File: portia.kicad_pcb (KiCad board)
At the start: 2 copper layers, 65.1 x 56.1 mm, 46 parts, among them J1 USB_B_Micro, J11 Conn_01x02, J12 Conn_01x02, J13 Conn_01x02, J14 Conn_01x02, J3 Conn_01x02, J7 Conn_01x02, SW1 Reset, U1 CP2102N-A01-GQFN24, U4 ESP32-WROOM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

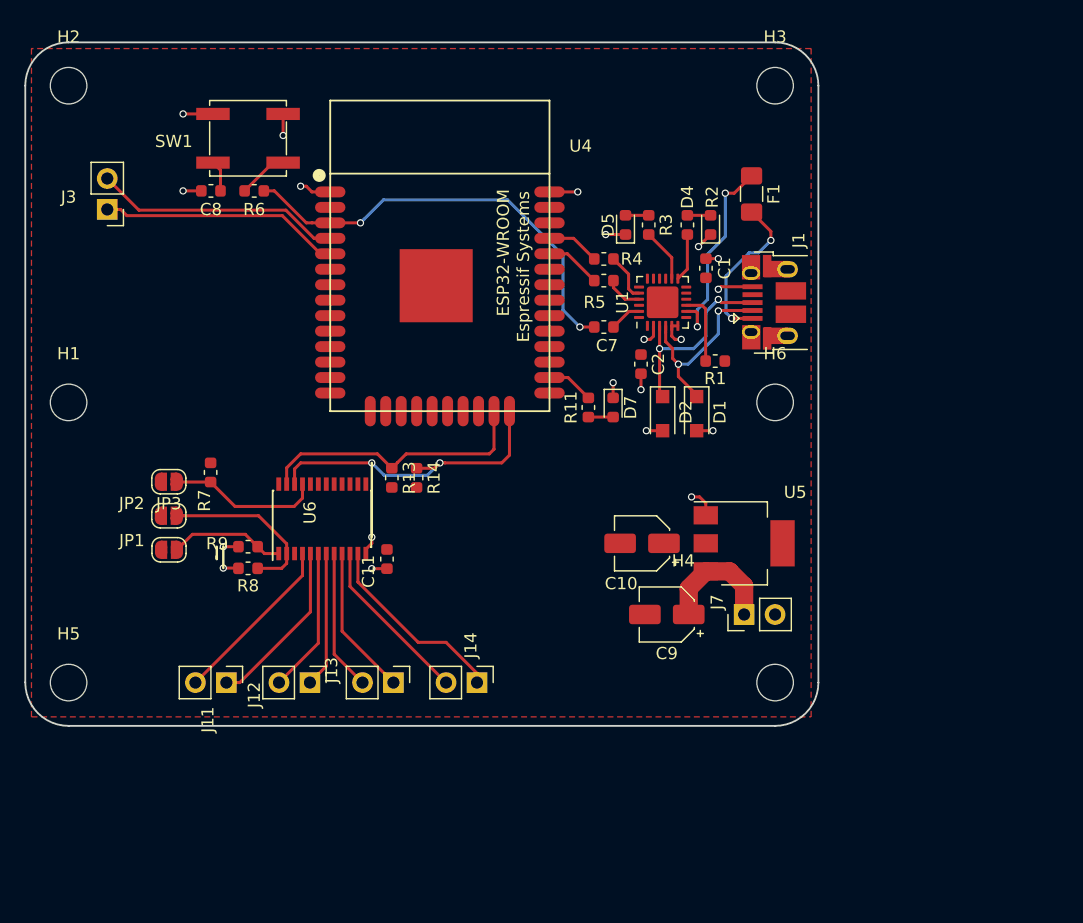
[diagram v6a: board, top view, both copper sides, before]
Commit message: adding new layout components
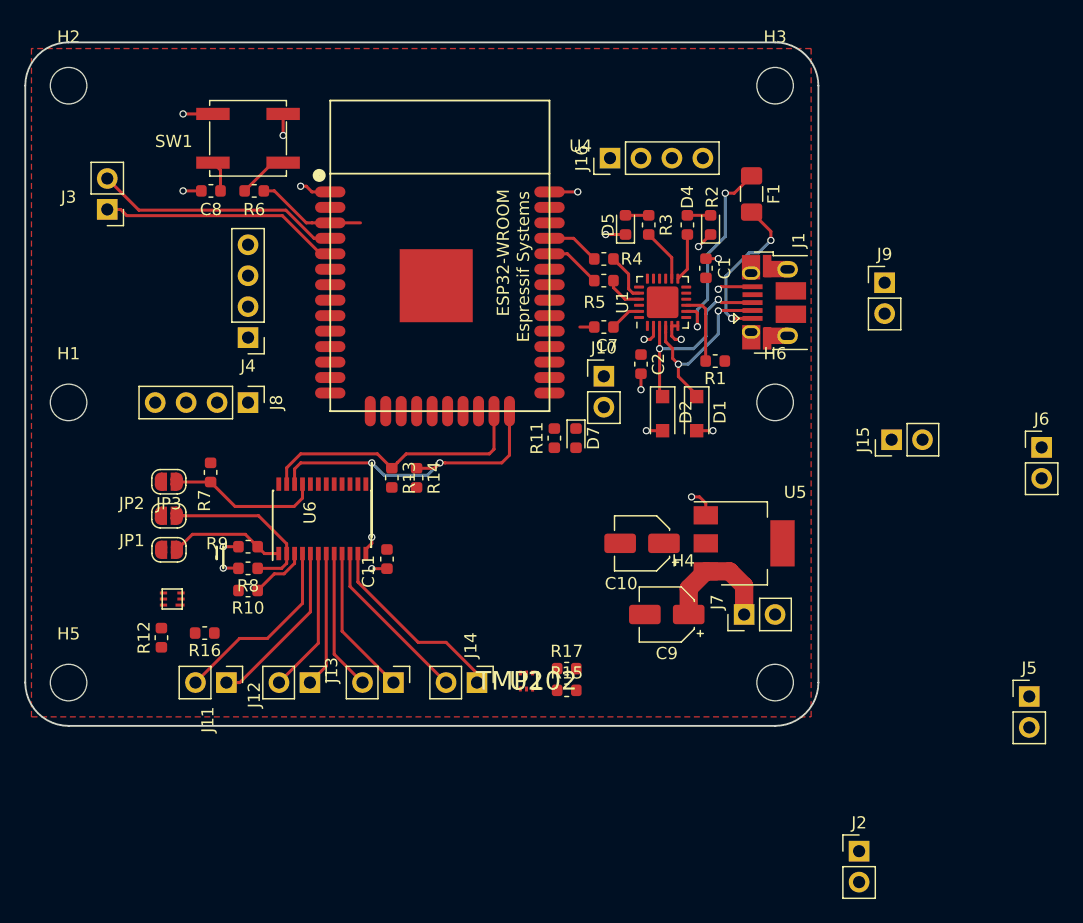
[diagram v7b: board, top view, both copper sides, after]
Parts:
- added J10: Conn_01x02, Connector_PinHeader_2.54mm:PinHeader_1x02_P2.54mm_Vertical, F.Cu at (204.0, 105.1)
- added J15: Conn_01x02, Connector_PinHeader_2.54mm:PinHeader_1x02_P2.54mm_Vertical, F.Cu at (227.6, 110.3)
- added J16: Conn_01x04, Connector_PinHeader_2.54mm:PinHeader_1x04_P2.54mm_Vertical, F.Cu at (204.5, 87.2)
- added J2: Conn_01x02, Connector_PinHeader_2.54mm:PinHeader_1x02_P2.54mm_Vertical, F.Cu at (224.9, 144.1)
- added J4: Conn_01x04, Connector_PinHeader_2.54mm:PinHeader_1x04_P2.54mm_Vertical, F.Cu at (174.8, 102.0)
- added J5: Conn_01x02, Connector_PinHeader_2.54mm:PinHeader_1x02_P2.54mm_Vertical, F.Cu at (238.9, 131.4)
- added J6: Conn_01x02, Connector_PinHeader_2.54mm:PinHeader_1x02_P2.54mm_Vertical, F.Cu at (239.9, 111.0)
- added J8: Conn_01x04, Connector_PinHeader_2.54mm:PinHeader_1x04_P2.54mm_Vertical, F.Cu at (174.8, 107.3)
- added J9: Conn_01x02, Connector_PinHeader_2.54mm:PinHeader_1x02_P2.54mm_Vertical, F.Cu at (227.0, 97.5)
- added M1: ISL29125, SparkFun-Sensors:ODFN-LD-6, F.Cu at (168.5, 123.4)
- added R10: R_Small, Resistor_SMD:R_0603_1608Metric, F.Cu at (174.8, 122.7)
- added R12: R_Small, Resistor_SMD:R_0603_1608Metric, F.Cu at (167.6, 126.6)
- added R15: R_Small, Resistor_SMD:R_0603_1608Metric, F.Cu at (200.9, 130.9)
- added R16: R_Small, Resistor_SMD:R_0603_1608Metric, F.Cu at (171.2, 126.2)
- added R17: R_Small, Resistor_SMD:R_0603_1608Metric, F.Cu at (200.9, 129.1)
- added U2: TMP102, SparkFun-Sensors:SOT563, F.Cu at (197.6, 130.2)
- moved D7 3.95 mm to (201.7, 110.2)
- moved R11 3.76 mm to (199.9, 110.2)
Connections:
- U4 pad 27: /rx -> Net-(J10-Pad2)
- U4 pad 28: /tx -> Net-(J10-Pad1)
- U4 pad 29: /cs -> Net-(J16-Pad4)
- U4 pad 30: /clk -> Net-(J16-Pad3)
- U4 pad 31: /miso -> Net-(J16-Pad2)
- U4 pad 33: /sda0 -> Net-(J9-Pad2)
- U4 pad 36: /scl0 -> Net-(J9-Pad1)
- U4 pad 37: /mosi -> Net-(J16-Pad1)
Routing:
- net /RESET: track 36.0 -> 10.2 mm, vias 2 -> 0
- net Net-(R10-Pad1): track 0.00 -> 4.76 mm
- net Net-(R11-Pad2): track 3.88 -> 0.00 mm
- net Net-(D7-Pad2): track 2.03 -> 0.00 mm
- net Net-(J11-Pad2): track 14.2 -> 15.6 mm
- net GND: track 32.7 -> 31.5 mm, vias 19 -> 18

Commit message: redesign layout sensors
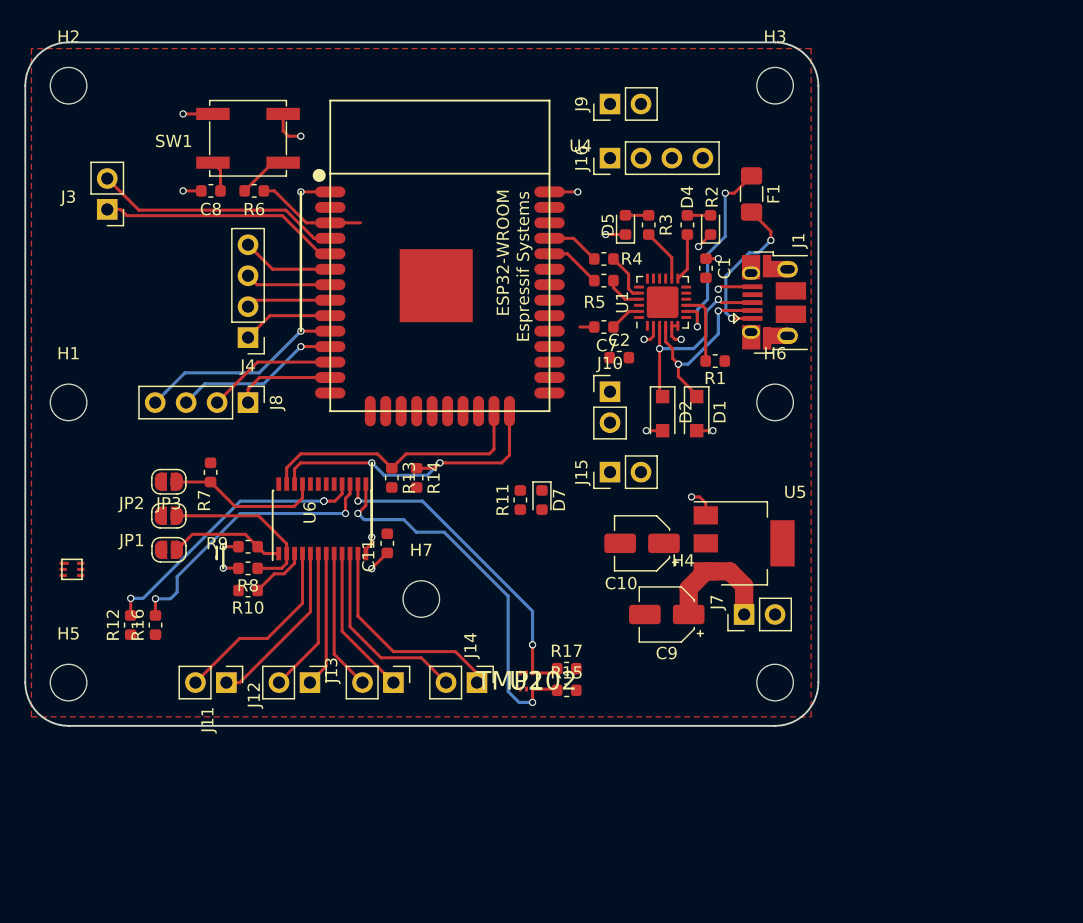
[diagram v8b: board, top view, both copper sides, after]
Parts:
- removed J2, J5, J6: Conn_01x02, Connector_PinHeader_2.54mm:PinHeader_1x02_P2.54mm_Vertical
- added H7: MountingHole, MountingHole:MountingHole_3mm, F.Cu at (189.0, 123.4)
- moved J9 26.9 mm to (204.5, 82.8), turned to 90 degrees
- moved J15 23.3 mm to (204.5, 113.0)
- moved M1 8.59 mm to (160.3, 121.0), turned to 0 degrees
- moved D7 5.80 mm to (198.9, 115.3)
- moved R11 5.80 mm to (197.1, 115.3)
- moved R16 4.10 mm to (167.2, 125.6), turned to 90 degrees
- moved R12 2.72 mm to (165.1, 125.6)
- moved C2 1.86 mm to (205.2, 103.6), turned to 0 degrees
- moved J10 1.37 mm to (204.5, 106.4)
- moved C11 1.29 mm to (186.2, 118.8)
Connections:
- U4 pad 10: Net-(J4-Pad2) -> Net-(J8-Pad4)
- U4 pad 11: Net-(J4-Pad1) -> Net-(J8-Pad3)
- U4 pad 12: Net-(J8-Pad4) -> Net-(J8-Pad2)
- U4 pad 13: Net-(J8-Pad3) -> Net-(J8-Pad1)
- U4 pad 14: Net-(J8-Pad2) -> Net-(U4-Pad14)
- U4 pad 16: Net-(J8-Pad1) -> Net-(U4-Pad16)
- U4 pad 6: Net-(J2-Pad2) -> Net-(J4-Pad4)
- U4 pad 7: Net-(J2-Pad1) -> Net-(J4-Pad3)
- U4 pad 8: Net-(J4-Pad4) -> Net-(J4-Pad2)
- U4 pad 9: Net-(J4-Pad3) -> Net-(J4-Pad1)
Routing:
- net Net-(R15-Pad1): track 0.00 -> 31.2 mm, vias 0 -> 2
- net Net-(R17-Pad1): track 0.00 -> 28.0 mm, vias 0 -> 2
- net Net-(M1-Pad4): track 0.00 -> 23.2 mm, vias 0 -> 2
- net Net-(M1-Pad6): track 0.00 -> 23.1 mm, vias 0 -> 3
- net Net-(J8-Pad4): track 0.00 -> 16.8 mm, vias 0 -> 1
- net Net-(J8-Pad3): track 0.00 -> 13.7 mm, vias 0 -> 1
- net Net-(J8-Pad2): track 0.00 -> 10.7 mm
- net Net-(J8-Pad1): track 0.00 -> 8.24 mm
- net Net-(J4-Pad3): track 0.00 -> 8.10 mm
- net Net-(J4-Pad4): track 0.00 -> 7.58 mm
- net Net-(J4-Pad1): track 0.00 -> 7.49 mm
- net Net-(J4-Pad2): track 0.00 -> 6.97 mm
- net Net-(J14-Pad2): track 13.9 -> 15.8 mm
- net Net-(J14-Pad1): track 16.0 -> 17.6 mm
- net GND: track 31.5 -> 32.7 mm, vias 18 -> 17
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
